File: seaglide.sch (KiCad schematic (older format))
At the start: 9 parts, among them U1 TSOP382xx

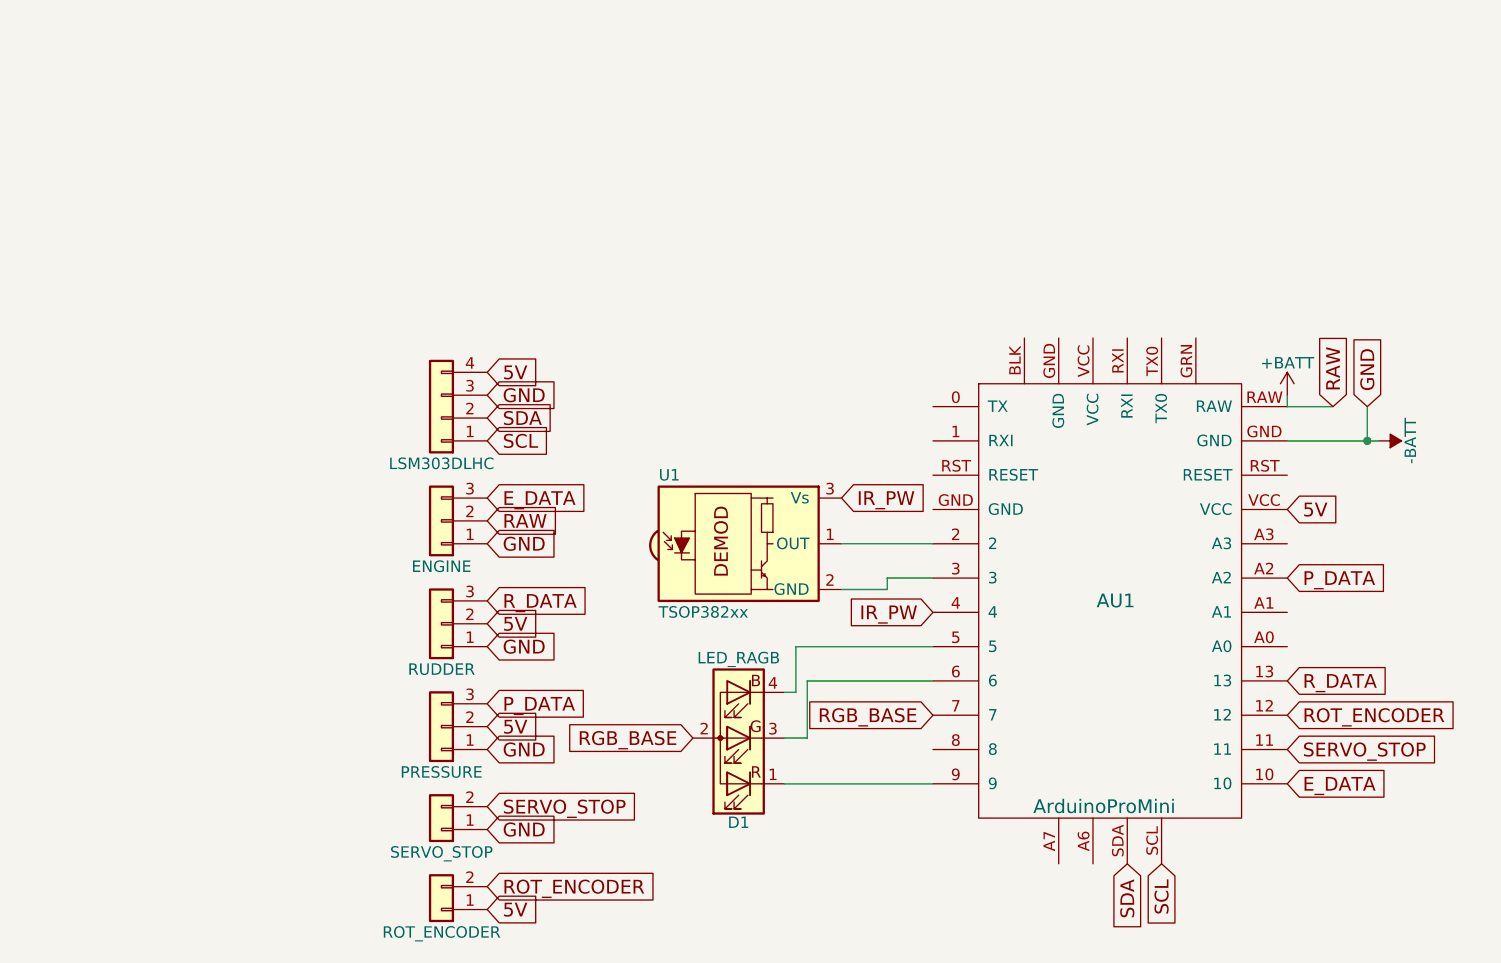
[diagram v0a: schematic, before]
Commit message: Fixed layout and added Desc
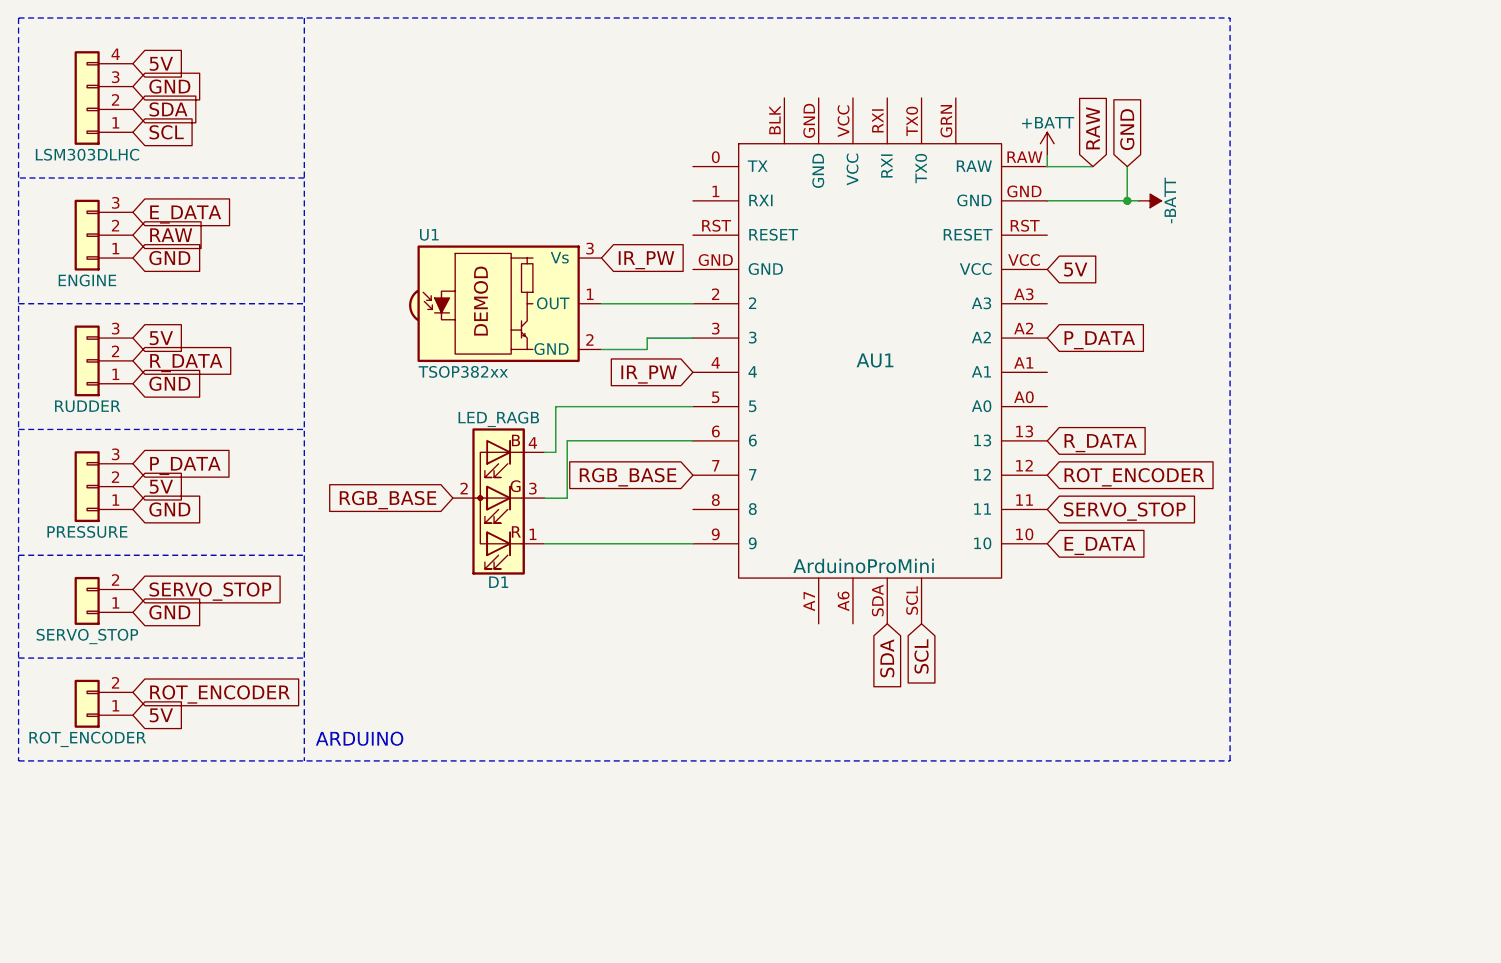
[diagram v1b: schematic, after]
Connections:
- net 5V: now also RUDDER.3 (Pin_3); no longer RUDDER.2 (Pin_2)
- net R_DATA: now also RUDDER.2 (Pin_2); no longer RUDDER.3 (Pin_3)
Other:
- note added: "ARDUINO"
- moved on the sheet: AU1, D1, ENGINE, LSM303DLHC, PRESSURE, ROT_ENCODER, RUDDER, SERVO_STOP, U1
